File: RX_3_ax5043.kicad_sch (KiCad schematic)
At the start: 21 parts, among them J4 2118714-2, P3 CONUFL001-SMD-T, Q5 DMP2037U, U17 AX5043

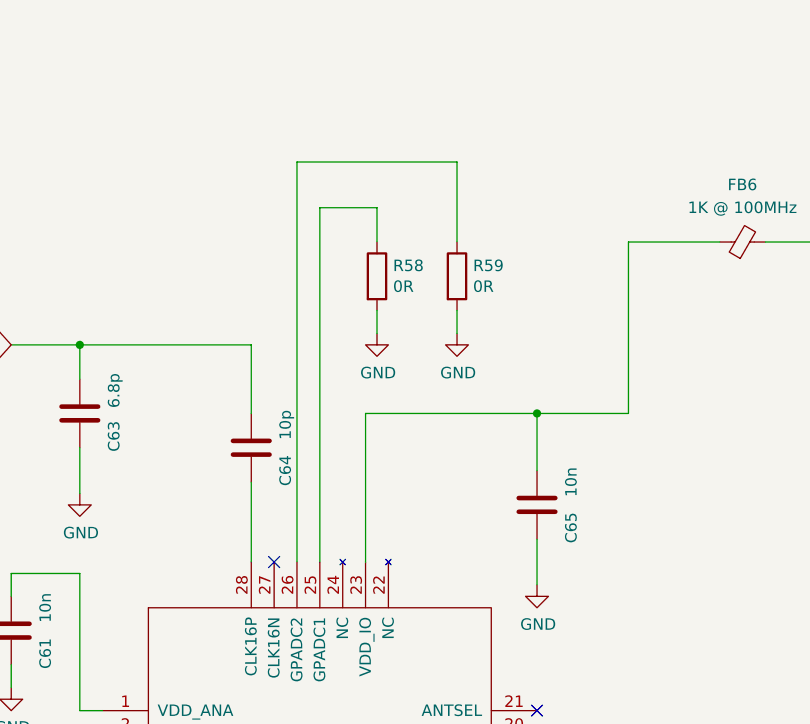
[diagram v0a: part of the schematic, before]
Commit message: More 0402 updates and cleanups
Signed-off-by: Corey Minyard <corey@minyard.net>
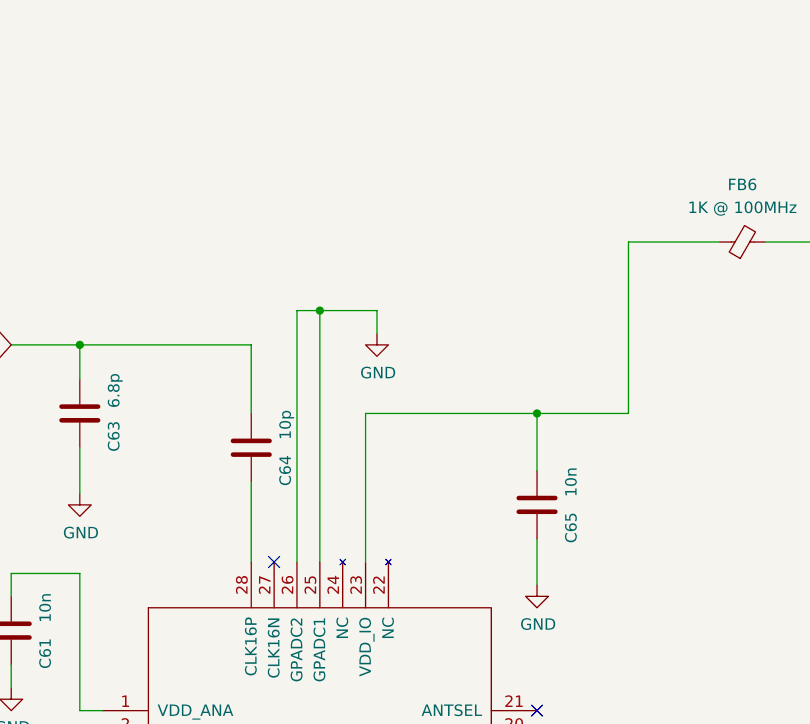
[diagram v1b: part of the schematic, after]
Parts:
- removed R58, R59: 0R, Resistor_SMD:R_0603_1608Metric_Pad0.98x0.95mm_HandSolder, symbol Device:R
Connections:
- net GND: now also U17.25 (GPADC1), U17.26 (GPADC2)
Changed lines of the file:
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@@
+	)
+	(junction
+		(at 269.24 72.39)
+		(diameter 0)
+		(color 0 0 0 0)
 	)
 	(junction
@@
 	(wire
 		(pts
-			(xy 269.24 60.96) (xy 275.59 60.96)
+			(xy 266.7 72.39) (xy 266.7 100.33)
 		)
 		(stroke
@@
 	(wire
 		(pts
-			(xy 284.48 55.88) (xy 284.48 64.77)
-		)
-		(stroke
-			(width 0)
-			(type default)
-		)
-	)
-	(wire
-		(pts
 			(xy 303.53 64.77) (xy 313.69 64.77)
 		)
@@
 	(wire
 		(pts
+			(xy 269.24 72.39) (xy 275.59 72.39)
+		)
+		(stroke
+			(width 0)
+			(type default)
+		)
+	)
+	(wire
+		(pts
 			(xy 163.83 44.45) (xy 168.91 44.45)
 		)
@@
 	(wire
 		(pts
-			(xy 269.24 60.96) (xy 269.24 100.33)
+			(xy 266.7 72.39) (xy 269.24 72.39)
 		)
 		(stroke
@@
 	(wire
 		(pts
+			(xy 269.24 72.39) (xy 269.24 100.33)
+		)
+		(stroke
+			(width 0)
+			(type default)
+		)
+	)
+	(wire
+		(pts
 			(xy 266.7 148.59) (xy 266.7 163.83)
 		)
@@
 	(wire
 		(pts
-			(xy 284.48 72.39) (xy 284.48 74.93)
-		)
-		(stroke
-			(width 0)
-			(type default)
-		)
-	)
-	(wire
-		(pts
 			(xy 172.72 127) (xy 172.72 128.27)
 		)
@@
 	(wire
 		(pts
-			(xy 266.7 55.88) (xy 284.48 55.88)
-		)
-		(stroke
-			(width 0)
-			(type default)
-		)
-	)
-	(wire
-		(pts
 			(xy 274.32 100.33) (xy 274.32 83.82)
 		)
@@
 	(wire
 		(pts
-			(xy 266.7 55.88) (xy 266.7 100.33)
-		)
-		(stroke
-			(width 0)
-			(type default)
-		)
-	)
-	(wire
-		(pts
 			(xy 222.25 138.43) (xy 222.25 140.97)
 		)
@@
 		(pts
 			(xy 264.16 148.59) (xy 264.16 153.67)
-		)
-		(stroke
-			(width 0)
-			(type default)
-		)
-	)
-	(wire
-		(pts
-			(xy 275.59 60.96) (xy 275.59 64.77)
 		)
 		(stroke
@@
 	)
 	(symbol
-		(lib_id "Device:R")
-		(at 275.59 68.58 0)
-		(unit 1)
-		(exclude_from_sim no)
-		(in_bom yes)
-		(on_board yes)
-		(dnp no)
-		(property "Reference" "R58"
-			(at 277.368 67.4116 0)
-			(effects
-				(font
-					(size 1.27 1.27)
-				)
-				(justify left)
-			)
-		)
-		(property "Value" "0R"
-			(at 277.368 69.723 0)
-			(effects
-				(font
-					(size 1.27 1.27)
-				)
-				(justify left)
-			)
-		)
-		(property "Footprint" "Resistor_SMD:R_0603_1608Metric_Pad0.98x0.95mm_HandSolder"
-			(at 273.812 68.58 90)
-			(effects
-				(font
-					(size 1.27 1.27)
-				)
-				(hide yes)
-			)
-		)
-		(property "Datasheet" "~"
-			(at 275.59 68.58 0)
-			(effects
-				(font
-					(size 1.27 1.27)
-				)
-			)
-		)
-		(property "Description" ""
-			(at 275.59 68.58 0)
-			(effects
-				(font
-					(size 1.27 1.27)
-				)
-			)
-		)
-		(pin "1"
-		)
-		(pin "2"
-		)
-		(instances
-			(project "PacSat_Dev_RevD_240614"
-				(path "/cc9f42d2-6985-41ac-acab-5ab7b01c5b38/d9a83ee4-3280-49b9-88b8-54d26cbd8ed1/6f28879f-0500-4efd-92c5-41e4c690888d"
-					(reference "R58")
-					(unit 1)
-				)
-			)
-		)
-	)
-	(symbol
 		(lib_id "Device:C")
 		(at 180.34 109.22 0)
@@
 				(path "/cc9f42d2-6985-41ac-acab-5ab7b01c5b38/d9a83ee4-3280-49b9-88b8-54d26cbd8ed1/6f28879f-0500-4efd-92c5-41e4c690888d"
 					(reference "#PWR0142")
-					(unit 1)
-				)
-			)
-		)
-	)
-	(symbol
-		(lib_id "power:GND")
-		(at 284.48 74.93 0)
-		(unit 1)
-		(exclude_from_sim no)
-		(in_bom yes)
-		(on_board yes)
-		(dnp no)
-		(property "Reference" "#PWR0148"
-			(at 284.48 81.28 0)
-			(effects
-				(font
-					(size 1.27 1.27)
-				)
-				(hide yes)
-			)
-		)
-		(property "Value" "GND"
-			(at 284.607 79.3242 0)
-			(effects
-				(font
-					(size 1.27 1.27)
-				)
-			)
-		)
-		(property "Footprint" ""
-			(at 284.48 74.93 0)
-			(effects
-				(font
-					(size 1.27 1.27)
-				)
-				(hide yes)
-			)
-		)
-		(property "Datasheet" ""
-			(at 284.48 74.93 0)
-			(effects
-				(font
-					(size 1.27 1.27)
-				)
-				(hide yes)
-			)
-		)
-		(property "Description" ""
-			(at 284.48 74.93 0)
-			(effects
-				(font
-					(size 1.27 1.27)
-				)
-			)
-		)
-		(pin "1"
-		)
-		(instances
-			(project "PacSat_Dev_RevD_240614"
-				(path "/cc9f42d2-6985-41ac-acab-5ab7b01c5b38/d9a83ee4-3280-49b9-88b8-54d26cbd8ed1/6f28879f-0500-4efd-92c5-41e4c690888d"
-					(reference "#PWR0148")
 					(unit 1)
 				)
@@
 					(unit 1)
 				)
-			)
-		)
-	)
-	(symbol
-		(lib_id "Device:R")
-		(at 284.48 68.58 0)
-		(unit 1)
-		(exclude_from_sim no)
-		(in_bom yes)
-		(on_board yes)
-		(dnp no)
-		(property "Reference" "R59"
-			(at 286.258 67.4116 0)
-			(effects
-				(font
-					(size 1.27 1.27)
-				)
-				(justify left)
-			)
-		)
-		(property "Value" "0R"
-			(at 286.258 69.723 0)
-			(effects
-				(font
-					(size 1.27 1.27)
-				)
-				(justify left)
-			)
-		)
-		(property "Footprint" "Resistor_SMD:R_0603_1608Metric_Pad0.98x0.95mm_HandSolder"
-			(at 282.702 68.58 90)
-			(effects
-				(font
-					(size 1.27 1.27)
-				)
-				(hide yes)
-			)
-		)
-		(property "Datasheet" "~"
-			(at 284.48 68.58 0)
-			(effects
-				(font
-					(size 1.27 1.27)
-				)
-			)
-		)
-		(property "Description" ""
-			(at 284.48 68.58 0)
-			(effects
-				(font
-					(size 1.27 1.27)
-				)
-			)
-		)
-		(pin "1"
-		)
-		(pin "2"
-		)
-		(instances
-			(project "PacSat_Dev_RevD_240614"
-				(path "/cc9f42d2-6985-41ac-acab-5ab7b01c5b38/d9a83ee4-3280-49b9-88b8-54d26cbd8ed1/6f28879f-0500-4efd-92c5-41e4c690888d"
-					(reference "R59")
-					(unit 1)
-				)

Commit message: Change appropriate passives to 0402 on the receive AX5043s
Signed-off-by: Corey Minyard <corey@minyard.net>
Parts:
- C58: footprint Resistor_SMD:R_0603_1608Metric_Pad0.98x0.95mm_HandSolder -> Capacitor_SMD:C_0402_1005Metric_Pad0.74x0.62mm_HandSolder
- C59, C60, C61, C62, C63, C64, C65: footprint Capacitor_SMD:C_0603_1608Metric_Pad1.08x0.95mm_HandSolder -> Capacitor_SMD:C_0402_1005Metric_Pad0.74x0.62mm_HandSolder
- R57, R60: footprint Resistor_SMD:R_0603_1608Metric_Pad0.98x0.95mm_HandSolder -> Resistor_SMD:R_0402_1005Metric_Pad0.72x0.64mm_HandSolder
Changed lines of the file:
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@@
 			)
 		)
-		(property "Footprint" "Resistor_SMD:R_0603_1608Metric_Pad0.98x0.95mm_HandSolder"
+		(property "Footprint" "Capacitor_SMD:C_0402_1005Metric_Pad0.74x0.62mm_HandSolder"
 			(at 181.3052 113.03 0)
 			(effects
@@
 			)
 		)
-		(property "Footprint" "Capacitor_SMD:C_0603_1608Metric_Pad1.08x0.95mm_HandSolder"
+		(property "Footprint" "Capacitor_SMD:C_0402_1005Metric_Pad0.74x0.62mm_HandSolder"
 			(at 189.23 129.2352 0)
 			(effects
@@
 			)
 		)
-		(property "Footprint" "Capacitor_SMD:C_0603_1608Metric_Pad1.08x0.95mm_HandSolder"
+		(property "Footprint" "Capacitor_SMD:C_0402_1005Metric_Pad0.74x0.62mm_HandSolder"
 			(at 239.7252 146.05 0)
 			(effects
@@
 			)
 		)
-		(property "Footprint" "Resistor_SMD:R_0603_1608Metric_Pad0.98x0.95mm_HandSolder"
+		(property "Footprint" "Resistor_SMD:R_0402_1005Metric_Pad0.72x0.64mm_HandSolder"
 			(at 304.8 133.858 90)
 			(effects
@@
 			)
 		)
-		(property "Footprint" "Capacitor_SMD:C_0603_1608Metric_Pad1.08x0.95mm_HandSolder"
+		(property "Footprint" "Capacitor_SMD:C_0402_1005Metric_Pad0.74x0.62mm_HandSolder"
 			(at 200.9648 130.81 0)
 			(effects
@@
 			)
 		)
-		(property "Footprint" "Capacitor_SMD:C_0603_1608Metric_Pad1.08x0.95mm_HandSolder"
+		(property "Footprint" "Capacitor_SMD:C_0402_1005Metric_Pad0.74x0.62mm_HandSolder"
 			(at 262.5852 91.44 0)
 			(effects
@@
 			)
 		)
-		(property "Footprint" "Capacitor_SMD:C_0603_1608Metric_Pad1.08x0.95mm_HandSolder"
+		(property "Footprint" "Capacitor_SMD:C_0402_1005Metric_Pad0.74x0.62mm_HandSolder"
 			(at 235.9152 111.76 0)
 			(effects
@@
 			)
 		)
-		(property "Footprint" "Resistor_SMD:R_0603_1608Metric_Pad0.98x0.95mm_HandSolder"
+		(property "Footprint" "Resistor_SMD:R_0402_1005Metric_Pad0.72x0.64mm_HandSolder"
 			(at 225.552 138.43 90)
 			(effects
@@
 			)
 		)
-		(property "Footprint" "Capacitor_SMD:C_0603_1608Metric_Pad1.08x0.95mm_HandSolder"
+		(property "Footprint" "Capacitor_SMD:C_0402_1005Metric_Pad0.74x0.62mm_HandSolder"
 			(at 294.3352 97.79 0)
 			(effects
@@
 			)
 		)
-		(property "Footprint" "Capacitor_SMD:C_0603_1608Metric_Pad1.08x0.95mm_HandSolder"
+		(property "Footprint" "Capacitor_SMD:C_0402_1005Metric_Pad0.74x0.62mm_HandSolder"
 			(at 243.5352 87.63 0)
 			(effects

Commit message: Work on cleaning up all values for things
Signed-off-by: Corey Minyard <corey@minyard.net>
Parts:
- C59, C60: value 15p -> 15p 1%
- L7, L8: value 78n -> 78n 2% Q=28
- L9: value 1n -> 1n Q=77; footprint Inductor_SMD:L_0603_1608Metric_Pad1.05x0.95mm_HandSolder -> Inductor_SMD:L_0402_1005Metric_Pad0.77x0.64mm_HandSolder
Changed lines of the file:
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@@
 			)
 		)
-		(property "Value" "78n"
+		(property "Value" "78n 2% Q=28"
 			(at 213.868 134.62 90)
 			(effects
@@
 			)
 		)
-		(property "Value" "15p"
+		(property "Value" "15p 1%"
 			(at 196.85 125.73 90)
 			(effects
@@
 			)
 		)
-		(property "Value" "15p"
+		(property "Value" "15p 1%"
 			(at 204.47 138.43 90)
 			(effects
@@
 			)
 		)
-		(property "Value" "78n"
+		(property "Value" "78n 2% Q=28"
 			(at 191.77 120.142 90)
 			(effects
@@
 			)
 		)
-		(property "Value" "1n"
+		(property "Value" "1n Q=77"
 			(at 223.774 134.366 90)
 			(effects
@@
 			)
 		)
-		(property "Footprint" "Inductor_SMD:L_0603_1608Metric_Pad1.05x0.95mm_HandSolder"
+		(property "Footprint" "Inductor_SMD:L_0402_1005Metric_Pad0.77x0.64mm_HandSolder"
 			(at 222.25 134.62 0)
 			(effects

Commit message: More work on components
Signed-off-by: Corey Minyard <corey@minyard.net>
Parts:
- FB6: value 1K @ 100MHz -> 1K@100MHz
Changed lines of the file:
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@@
 			)
 		)
-		(property "Value" "1K @ 100MHz"
+		(property "Value" "1K@100MHz"
 			(at 316.1919 60.96 90)
 			(effects

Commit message: Lots of updates to ease manufacturing
Component changes, changes in the formatting of the values, etc.

Signed-off-by: Corey Minyard <corey@minyard.net>
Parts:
- C58: value 100p -> 100pF
- C59, C60: value 15p 1% -> 15pF 1%
- C61, C62, C65: value 10n -> 10nF
- C63: value 6.8p -> 6.8pF
- C64: value 10p -> 10pF
- L7, L8: value 78n 2% Q=28 -> 78nH 2% Q=28
- L9: value 1n Q=77 -> 1nH Q=77
- Q5: value DMP2037U -> DMP2037U-7
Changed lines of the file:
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@@
 			)
 		)
-		(property "Value" "100p"
+		(property "Value" "100pF"
 			(at 183.134 110.5154 0)
 			(effects
@@
 			)
 		)
-		(property "Value" "78n 2% Q=28"
+		(property "Value" "78nH 2% Q=28"
 			(at 213.868 134.62 90)
 			(effects
@@
 			)
 		)
-		(property "Value" "15p 1%"
+		(property "Value" "15pF 1%"
 			(at 196.85 125.73 90)
 			(effects
@@
 			)
 		)
-		(property "Value" "10n"
+		(property "Value" "10nF"
 			(at 236.22 138.43 90)
 			(effects
@@
 			)
 		)
-		(property "Value" "DMP2037U"
+		(property "Value" "DMP2037U-7"
 			(at 334.01 60.96 90)
 			(effects
@@
 			)
 		)
-		(property "Value" "15p 1%"
+		(property "Value" "15pF 1%"
 			(at 204.47 138.43 90)
 			(effects
@@
 			)
 		)
-		(property "Value" "10p"
+		(property "Value" "10pF"
 			(at 265.43 85.09 90)
 			(effects
@@
 			)
 		)
-		(property "Value" "10n"
+		(property "Value" "10nF"
 			(at 238.76 105.41 90)
 			(effects
@@
 			)
 		)
-		(property "Value" "78n 2% Q=28"
+		(property "Value" "78nH 2% Q=28"
 			(at 191.77 120.142 90)
 			(effects
@@
 			)
 		)
-		(property "Value" "1n Q=77"
+		(property "Value" "1nH Q=77"
 			(at 223.774 134.366 90)
 			(effects
@@
 			)
 		)
-		(property "Value" "10n"
+		(property "Value" "10nF"
 			(at 297.18 91.44 90)
 			(effects
@@
 			)
 		)
-		(property "Value" "6.8p"
+		(property "Value" "6.8pF"
 			(at 246.38 81.28 90)
 			(effects

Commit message: Update all resistors to have an ohm symbol
Make it more clean in the BOM what they are.

Signed-off-by: Corey Minyard <corey@minyard.net>
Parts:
- R57: value 50 -> 50Ω
- R60: value 470 -> 470Ω
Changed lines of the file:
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@@
 			)
 		)
-		(property "Value" "470"
+		(property "Value" "470Ω"
 			(at 305.054 136.906 90)
 			(effects
@@
 			)
 		)
-		(property "Value" "50"
+		(property "Value" "50Ω"
 			(at 229.108 139.573 0)
 			(effects

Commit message: Massive rework of filtering and inductors
Now that I know how inductors really work.

Signed-off-by: Corey Minyard <corey@minyard.net>
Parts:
- L7, L8: value 78nH 2% Q=28 -> 78nH 2%
- L9: value 1nH Q=77 -> 1nH
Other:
- note removed: "See RX1 for Q values on inductors."
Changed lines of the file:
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@@
-		)
-	)
-	(text "See RX1 for Q values on inductors."
-		(exclude_from_sim no)
-		(at 177.546 165.862 0)
-		(effects
-			(font
-				(size 1.524 1.524)
-			)
-			(justify left bottom)
 		)
 	)
@@
 			)
 		)
-		(property "Value" "78nH 2% Q=28"
+		(property "Value" "78nH 2%"
 			(at 213.868 134.62 90)
 			(effects
@@
 			)
 		)
-		(property "Value" "78nH 2% Q=28"
+		(property "Value" "78nH 2%"
 			(at 191.77 120.142 90)
 			(effects
@@
 			)
 		)
-		(property "Value" "1nH Q=77"
+		(property "Value" "1nH"
 			(at 223.774 134.366 90)
 			(effects

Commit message: Have the BOM file fixer output xls, not csv
The omega symbol gets translated properly from xls.

Signed-off-by: Corey Minyard <corey@minyard.net>
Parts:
- FB6: footprint Resistor_SMD:R_0603_1608Metric_Pad0.98x0.95mm_HandSolder -> Inductor_SMD:L_0603_1608Metric_Pad1.05x0.95mm_HandSolder
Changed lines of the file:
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@@
 			)
 		)
-		(property "Footprint" "Resistor_SMD:R_0603_1608Metric_Pad0.98x0.95mm_HandSolder"
+		(property "Footprint" "Inductor_SMD:L_0603_1608Metric_Pad1.05x0.95mm_HandSolder"
 			(at 316.23 66.548 90)
 			(effects
